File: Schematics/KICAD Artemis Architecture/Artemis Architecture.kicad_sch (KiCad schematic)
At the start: 0 parts

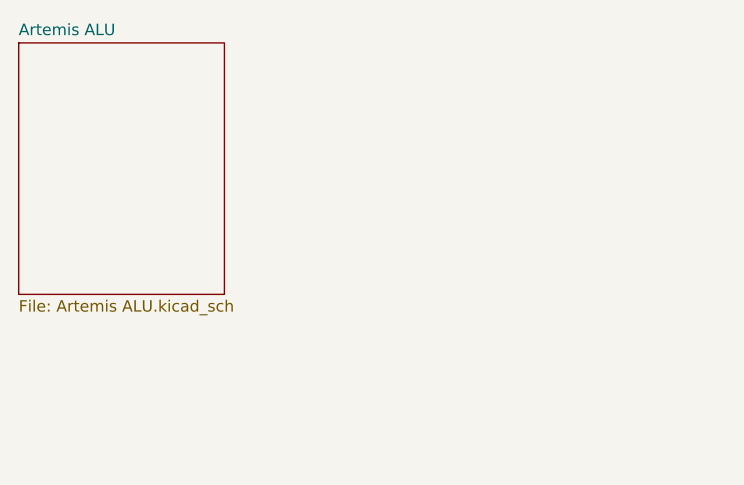
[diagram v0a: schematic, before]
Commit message: Began refactoring schematics for the 74ls181 ALU
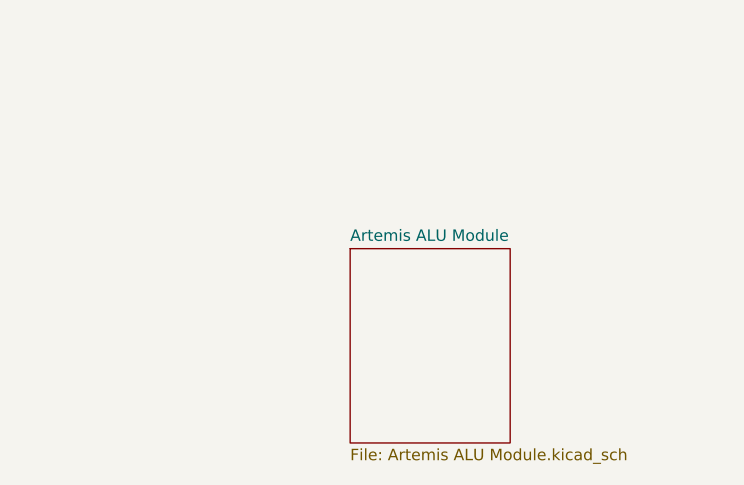
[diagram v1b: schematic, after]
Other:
- removed sheet Artemis ALU
- added sheet Artemis ALU Module (Artemis ALU Module.kicad_sch)
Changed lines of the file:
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@@
 	(paper "A4")
 	(sheet
-		(at 109.22 66.04)
-		(size 22.86 27.94)
+		(at 146.05 88.9)
+		(size 17.78 21.59)
 		(fields_autoplaced yes)
 		(stroke
@@
 			(color 0 0 0 0.0000)
 		)
-		(property "Sheetname" "Artemis ALU"
-			(at 109.22 65.3284 0)
-			(show_name yes)
+		(property "Sheetname" "Artemis ALU Module"
+			(at 146.05 88.1884 0)
 			(effects
 				(font
@@
 			)
 		)
-		(property "Sheetfile" "Artemis ALU.kicad_sch"
-			(at 109.22 94.5646 0)
+		(property "Sheetfile" "Artemis ALU Module.kicad_sch"
+			(at 146.05 111.0746 0)
 			(effects
 				(font

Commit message: Added ALU Module PCB
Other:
- sheet Artemis ALU Module ports: added A0, A1, A2, A3, A4, A5, A6, A7, B0, B1, B2, B3, B4, B5, B6, B7, F0, F1, F2, F3, F4, F5, F6, F7, M, S0, S1, S2, S3, Zero flag, ~{Carry flag}, ~{Cn}; removed none
- company: (none) -> George Sleen
- title: (none) -> Artemis

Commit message: Register PCB Created and Finished
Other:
- added sheet Register A (Artemis Register Module.kicad_sch)
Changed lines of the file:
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@@
+		)
+	)
+	(sheet
+		(at 605.79 251.46)
+		(size 12.7 3.81)
+		(fields_autoplaced yes)
+		(stroke
+			(width 0.1524)
+			(type solid)
+		)
+		(fill
+			(color 0 0 0 0.0000)
+		)
+		(property "Sheetname" "Register A"
+			(at 605.79 250.7484 0)
+			(effects
+				(font
+					(size 1.27 1.27)
+				)
+				(justify left bottom)
+			)
+		)
+		(property "Sheetfile" "Artemis Register Module.kicad_sch"
+			(at 605.79 255.8546 0)
+			(effects
+				(font
+					(size 1.27 1.27)
+				)
+				(justify left top)
+			)
+		)
+		(instances
+			(project "Artemis Architecture"
+				(path "/e5aa38bc-c1b3-42af-8692-454c67b5224c"
+					(page "3")
+				)
+			)
 		)
 	)
